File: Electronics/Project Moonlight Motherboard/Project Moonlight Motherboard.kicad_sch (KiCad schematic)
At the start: 40 parts, among them M1 AO3400A, M2 AO3400A, M3 AO3400A, U1 Pico, U2 TMC2209_SILENTSTEPSTICK, U3 TMC2209_SILENTSTEPSTICK, U4 TMC2209_SILENTSTEPSTICK, U5 TMC2209_SILENTSTEPSTICK

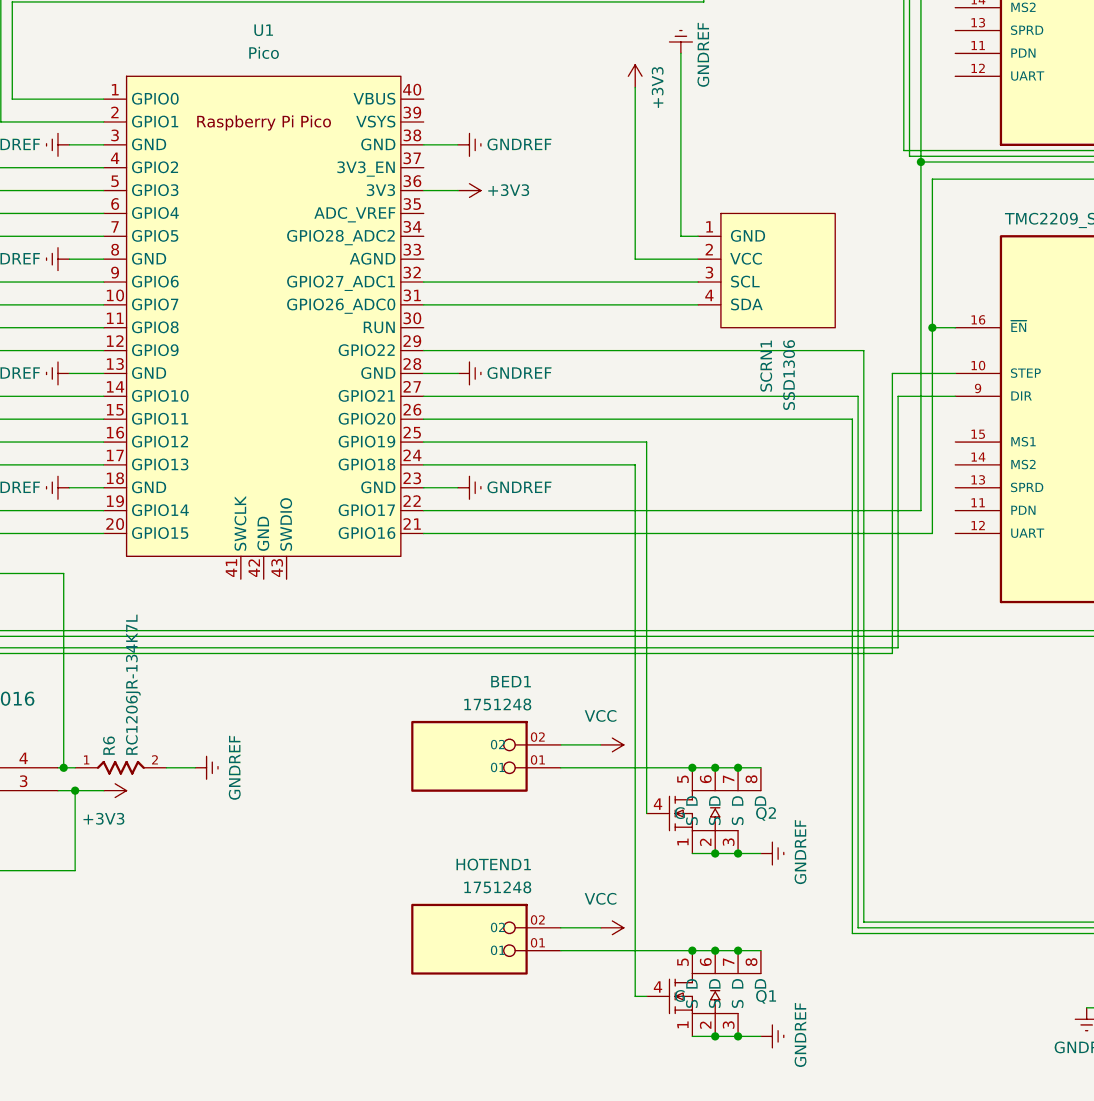
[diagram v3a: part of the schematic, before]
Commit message: added a random resistor for UART - coming soon...
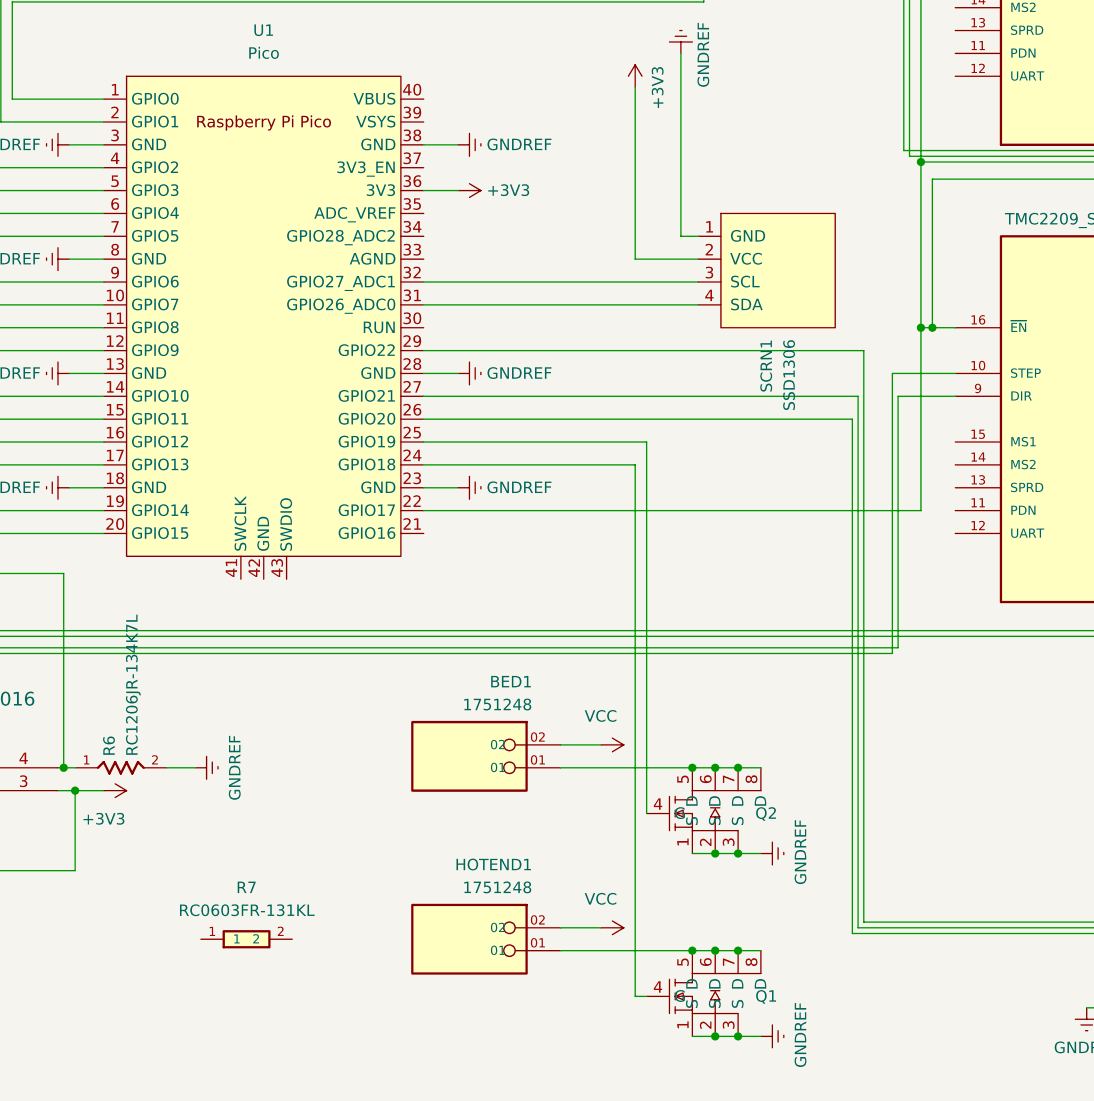
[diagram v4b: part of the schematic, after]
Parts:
- added R7: RC0603FR-131KL, RC0603FR-131KL:0603, symbol RC0603FR-131KL:RC0603FR-131KL
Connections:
- net at U1.22 (GPIO17), U2.16 (~{EN}), U3.16 (~{EN}): now also U4.16 (~{EN}), U5.16 (~{EN})
- now unconnected: U1.21 (GPIO16)
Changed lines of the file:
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@@
   (junction (at 275.59 145.415) (diameter 0) (color 0 0 0 0)
   )
+  (junction (at 298.45 96.52) (diameter 0) (color 0 0 0 0)
+  )
   (junction (at 394.97 91.44) (diameter 0) (color 0 0 0 0)
   )
@@
     (stroke (width 0) (type default))
   )
-  (wire (pts (xy 298.45 78.105) (xy 298.45 116.84))
+  (wire (pts (xy 298.45 78.105) (xy 298.45 96.52))
     (stroke (width 0) (type default))
   )
@@
     (stroke (width 0) (type default))
   )
-  (wire (pts (xy 299.72 119.38) (xy 243.205 119.38))
-    (stroke (width 0) (type default))
-  )
   (wire (pts (xy 338.455 124.46) (xy 341.63 124.46))
     (stroke (width 0) (type default))
@@
     (stroke (width 0) (type default))
   )
-  (wire (pts (xy 299.72 96.52) (xy 299.72 119.38))
-    (stroke (width 0) (type default))
-  )
   (wire (pts (xy 147.955 71.755) (xy 179.07 71.755))
     (stroke (width 0) (type default))
@@
     (stroke (width 0) (type default))
   )
+  (wire (pts (xy 298.45 96.52) (xy 298.45 116.84))
+    (stroke (width 0) (type default))
+  )
   (wire (pts (xy 207.645 114.3) (xy 203.835 114.3))
     (stroke (width 0) (type default))
@@
   )
   (wire (pts (xy 273.05 145.415) (xy 275.59 145.415))
+    (stroke (width 0) (type default))
+  )
+  (wire (pts (xy 298.45 96.52) (xy 299.72 96.52))
     (stroke (width 0) (type default))
   )
@@
     (pin "2")
     (pin "3")
+    (pin "3")
     (pin "4")
-    (pin "3")
     (instances
       (project "Project Moonlight Motherboard"
@@
         )
       )
+    )
+  )
+  (symbol (lib_id "RC0603FR-131KL:RC0603FR-131KL") (at 223.52 164.465 0) (unit 1)
+    (in_bom yes) (on_board yes) (dnp no) (fields_autoplaced)
+    (property "Reference" "R7" (at 223.52 158.75 0)
+      (effects (font (size 1.27 1.27)))
+    )
+    (property "Value" "RC0603FR-131KL" (at 223.52 161.29 0)
+      (effects (font (size 1.27 1.27)))
+    )
+    (property "Footprint" "RC0603FR-131KL:0603" (at 223.52 164.465 0)
+      (effects (font (size 1.27 1.27)) (justify bottom) hide)
+    )
+    (property "Datasheet" "" (at 223.52 164.465 0)
+      (effects (font (size 1.27 1.27)) hide)
+    )
+    (property "DigiKey_Part_Number" "13-RC0603FR-131KLTR-ND" (at 223.52 164.465 0)
+      (effects (font (size 1.27 1.27)) (justify bottom) hide)
+    )
+    (property "MF" "Yageo" (at 223.52 164.465 0)
+      (effects (font (size 1.27 1.27)) (justify bottom) hide)
+    )
+    (property "Purchase-URL" "https://www.snapeda.com/api/url_track_click_mouser/?unipart_id=47010&manufacturer=Yageo&part_name=RC0603FR-131KL&search_term=None" (at 223.52 164.465 0)
+      (effects (font (size 1.27 1.27)) (justify bottom) hide)
+    )
+    (property "Package" "0603 Yageo" (at 223.52 164.465 0)
+      (effects (font (size 1.27 1.27)) (justify bottom) hide)
+    )
+    (property "SnapEDA_Link" "https://www.snapeda.com/parts/RC0603FR-131KL/Yageo/view-part/?ref=snap" (at 223.52 164.465 0)
+      (effects (font (size 1.27 1.27)) (justify bottom) hide)
+    )
+    (property "MP" "RC0603FR-131KL" (at 223.52 164.465 0)
+      (effects (font (size 1.27 1.27)) (justify bottom) hide)
+    )
+    (property "Description" "\n1 kOhms ±1% 0.1W, 1/10W Chip Resistor 0603 (1608 Metric) Moisture Resistant Thick Film\n" (at 223.52 164.465 0)
+      (effects (font (size 1.27 1.27)) (justify bottom) hide)
+    )
+    (property "Check_prices" "https://www.snapeda.com/parts/RC0603FR-131KL/Yageo/view-part/?ref=eda" (at 223.52 164.465 0)
+      (effects (font (size 1.27 1.27)) (justify bottom) hide)
+    )
+    (pin "1")
+    (pin "2")
+    (instances
+      (project "Project Moonlight Motherboard"
+        (path "/9290e430-09f5-4a3f-8744-4071dceedc2e"
+          (reference "R7") (unit 1)
+        )
+      )
